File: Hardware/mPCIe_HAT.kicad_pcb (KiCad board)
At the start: 4 copper layers, 65 x 56.8 mm, 134 parts, among them J25 jumper, J4 EMCON_HEADER_1x2-, J5 jumper, K1 USB_C_Receptacle_USB2.0, M1 MPCIE_LATCH, P1 EMCON_RPI_GPIO_HEADER_2x20, Q2 BC856BS, Q3 DMP3013SFV, SW1 SW_Push

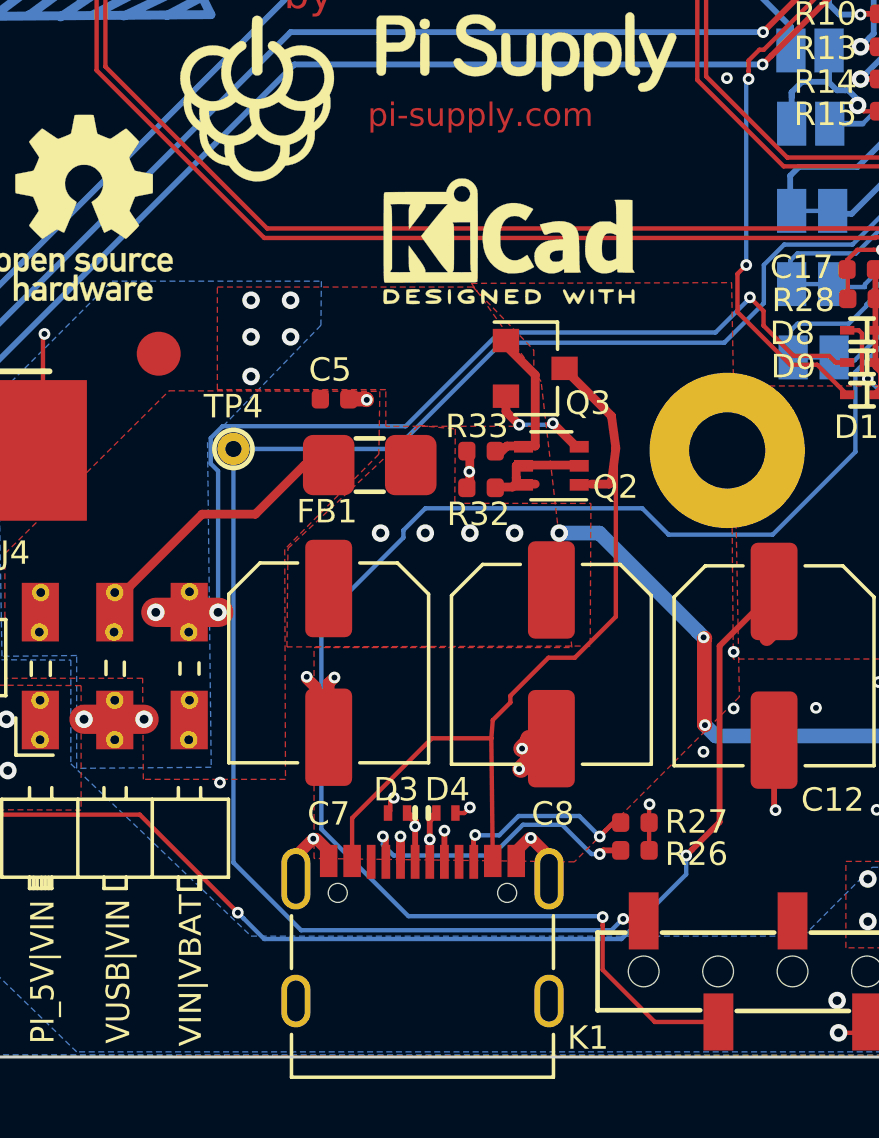
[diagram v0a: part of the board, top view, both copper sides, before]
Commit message: Q2B connection fix, position file generated.
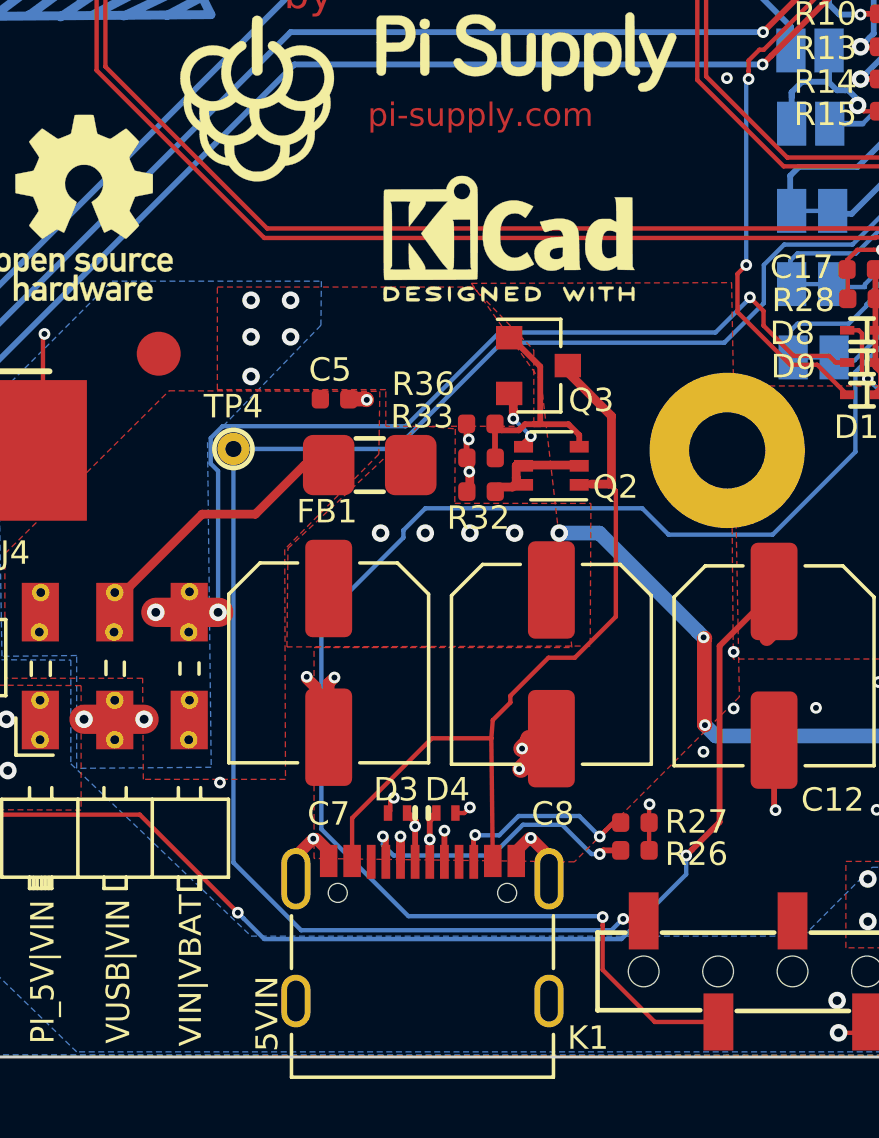
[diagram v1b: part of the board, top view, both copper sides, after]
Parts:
- added R36: 62K, Resistor_SMD:R_0402_1005Metric, F.Cu at (141.0, 106.2)
- C5: value 33pF -> 100nF
- moved R33 0.23 mm to (141.0, 107.4)
- moved Q3 0.15 mm to (143.0, 104.2)
- moved R32 0.13 mm to (141.0, 108.5)
- moved LG8 0.09 mm to (141.9, 99.9)
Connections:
- Q2 pad 3: /VUSB -> Net-(Q2-Pad3)
- Q2 pad 4: Net-(Q2-Pad4) -> /VUSB
- Q3 pad 1: Net-(Q2-Pad4) -> Net-(Q2-Pad3)
- R33 pad 2: Net-(Q2-Pad4) -> Net-(Q2-Pad3)
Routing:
- net Net-(Q2-Pad3): track 0.00 -> 8.54 mm
- net Net-(Q2-Pad4): track 5.40 -> 0.00 mm
- net /VUSB: track 5.61 -> 4.23 mm
- net GND: track 108.0 -> 109.2 mm, vias 117 -> 118
- net /VBUS: track 29.0 -> 27.8 mm
- net Net-(Q2-Pad2): track 4.10 -> 3.47 mm
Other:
- board text added: "5VIN"
